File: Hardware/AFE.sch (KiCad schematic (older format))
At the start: 42 parts, among them U801 4069.HEF4069UBTT,118, U802 MCP47CXBX2

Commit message: Trying to add suppliers in Altium formats.
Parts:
- C701, C802, C804, C815, C816, C820, C822: Supplier 1 (none) -> Digi-Key; Supplier Part Number 1 (none) -> 399-6856-1-ND
- D801, D802: Supplier 1 (none) -> Mouser; Supplier Part Number 1 (none) -> 726-BB914E6327
- L801, L802: Supplier 1 (none) -> Mouser; Supplier Part Number 1 (none) -> 810-NL453232T-102JPF
- R801, R802, R803, R804, R809: Supplier 1 (none) -> Digi-Key; Supplier Part Number 1 (none) -> RHM100KDCT-ND
- U801: Supplier 1 (none) -> Digi-Key; Supplier Part Number 1 (none) -> 1727-6749-1-ND
- U801: DPN (none) -> 1727-6749-1-ND; Supplier 1 (none) -> Digi-Key; Supplier Part Number 1 (none) -> 1727-6749-1-ND
- U802: Supplier 1 (none) -> Digi-Key; Supplier Part Number 1 (none) -> MCP47CMB02-E/MF-ND
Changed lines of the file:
@@
 F 2 "OHMC2022:TSSOP14" H 3200 4550 60  0001 C CNN
 F 3 "https://assets.nexperia.com/documents/data-sheet/HEF4069UB.pdf" H 3200 4550 60  0001 C CNN
+F 4 "1727-6749-1-ND" H 3200 4550 50  0001 C CNN "DPN"
+F 5 "Digi-Key" H 3200 4550 50  0001 C CNN "Supplier 1"
+F 6 "1727-6749-1-ND" H 3200 4550 50  0001 C CNN "Supplier Part Number 1"
 	2    3200 4550
 	1    0    0    -1
@@
 F 4 "1727-6749-1-ND" H 2050 4550 50  0001 C CNN "DPN"
 F 5 "HEF4069UBTT,118" H 2050 4550 50  0001 C CNN "MPN"
+F 6 "Digi-Key" H 2050 4550 50  0001 C CNN "Supplier 1"
+F 7 "1727-6749-1-ND" H 2050 4550 50  0001 C CNN "Supplier Part Number 1"
 	3    2050 4550
 	1    0    0    -1
@@
 F 4 "NL453232T-102J-PF " H 2100 1800 50  0001 C CNN "MPN"
 F 5 "810-NL453232T-102JPF" H 2100 1800 50  0001 C CNN "MouserPN"
+F 6 "Mouser" H 2100 1800 50  0001 C CNN "Supplier 1"
+F 7 "810-NL453232T-102JPF" H 2100 1800 50  0001 C CNN "Supplier Part Number 1"
 	1    2100 1800
 	1    0    0    -1
@@
 F 4 "1727-6749-1-ND" H 3200 5250 50  0001 C CNN "DPN"
 F 5 "HEF4069UBTT,118" H 3200 5250 50  0001 C CNN "MPN"
+F 6 "Digi-Key" H 3200 5250 50  0001 C CNN "Supplier 1"
+F 7 "1727-6749-1-ND" H 3200 5250 50  0001 C CNN "Supplier Part Number 1"
 	1    3200 5250
 	1    0    0    -1
@@
 F 4 "BB 914 E6327 " H 1050 2900 50  0001 C CNN "MPN"
 F 5 "726-BB914E6327 " H 1050 2900 50  0001 C CNN "MouserPN"
+F 6 "Mouser" H 1050 2900 50  0001 C CNN "Supplier 1"
+F 7 "726-BB914E6327" H 1050 2900 50  0001 C CNN "Supplier Part Number 1"
 	1    1050 2900
 	1    0    0    -1
@@
 F 2 "OHMC2022:TSSOP14" H 3200 1100 60  0001 C CNN
 F 3 "https://assets.nexperia.com/documents/data-sheet/HEF4069UB.pdf" H 3200 1100 60  0001 C CNN
+F 4 "1727-6749-1-ND" H 3200 1100 50  0001 C CNN "DPN"
+F 5 "Digi-Key" H 3200 1100 50  0001 C CNN "Supplier 1"
+F 6 "1727-6749-1-ND" H 3200 1100 50  0001 C CNN "Supplier Part Number 1"
 	5    3200 1100
 	1    0    0    -1
@@
 F 2 "OHMC2022:TSSOP14" H 3200 1800 60  0001 C CNN
 F 3 "https://assets.nexperia.com/documents/data-sheet/HEF4069UB.pdf" H 3200 1800 60  0001 C CNN
+F 4 "1727-6749-1-ND" H 3200 1800 50  0001 C CNN "DPN"
+F 5 "Digi-Key" H 3200 1800 50  0001 C CNN "Supplier 1"
+F 6 "1727-6749-1-ND" H 3200 1800 50  0001 C CNN "Supplier Part Number 1"
 	6    3200 1800
 	1    0    0    -1
@@
 F 2 "OHMC2022:TSSOP14" H 2050 1100 60  0001 C CNN
 F 3 "https://assets.nexperia.com/documents/data-sheet/HEF4069UB.pdf" H 2050 1100 60  0001 C CNN
+F 4 "1727-6749-1-ND" H 2050 1100 50  0001 C CNN "DPN"
+F 5 "Digi-Key" H 2050 1100 50  0001 C CNN "Supplier 1"
+F 6 "1727-6749-1-ND" H 2050 1100 50  0001 C CNN "Supplier Part Number 1"
 	4    2050 1100
 	1    0    0    -1
@@
 F 4 "MCP47CMB02-E/MF-ND" H 7900 5000 50  0001 C CNN "DPN"
 F 5 "MCP47CMB02-E/MF" H 7850 4850 50  0001 C CNN "MPN"
+F 6 "Digi-Key" H 7450 4400 50  0001 C CNN "Supplier 1"
+F 7 "MCP47CMB02-E/MF-ND" H 7450 4400 50  0001 C CNN "Supplier Part Number 1"
 	1    7450 4400
 	1    0    0    -1
@@
 F 4 "BB 914 E6327 " H 1050 6350 50  0001 C CNN "MPN"
 F 5 "726-BB914E6327 " H 1050 6350 50  0001 C CNN "MouserPN"
+F 6 "Mouser" H 1050 6350 50  0001 C CNN "Supplier 1"
+F 7 "726-BB914E6327" H 1050 6350 50  0001 C CNN "Supplier Part Number 1"
 	1    1050 6350
 	1    0    0    -1
@@
 F 4 "NL453232T-102J-PF " H 2100 5250 50  0001 C CNN "MPN"
 F 5 "810-NL453232T-102JPF" H 2100 5250 50  0001 C CNN "MouserPN"
+F 6 "Mouser" H 2100 5250 50  0001 C CNN "Supplier 1"
+F 7 "810-NL453232T-102JPF" H 2100 5250 50  0001 C CNN "Supplier Part Number 1"
 	1    2100 5250
 	1    0    0    -1
@@
 F 4 "HEF4069UBTT,118" H 9000 1350 50  0001 C CNN "MPN"
 F 5 "1727-6749-1-ND" H 9000 1350 50  0001 C CNN "DPN"
+F 6 "Digi-Key" H 9000 1350 50  0001 C CNN "Supplier 1"
+F 7 "1727-6749-1-ND" H 9000 1350 50  0001 C CNN "Supplier Part Number 1"
 	7    9000 1350
 	1    0    0    -1
@@
 F 5 "ESR03EZPJ104" H 1450 3550 50  0001 C CNN "MPN"
 F 6 "RHM100KDCT-ND" H 1450 3550 50  0001 C CNN "DPN"
+F 7 "Digi-Key" H 1450 3550 50  0001 C CNN "Supplier 1"
+F 8 "RHM100KDCT-ND" H 1450 3550 50  0001 C CNN "Supplier Part Number 1"
 	1    1450 3550
 	0    -1   -1   0
@@
 F 5 "ESR03EZPJ104" H 1050 3300 50  0001 C CNN "MPN"
 F 6 "RHM100KDCT-ND" H 1050 3300 50  0001 C CNN "DPN"
+F 7 "Digi-Key" H 1050 3300 50  0001 C CNN "Supplier 1"
+F 8 "RHM100KDCT-ND" H 1050 3300 50  0001 C CNN "Supplier Part Number 1"
 	1    1050 3300
 	1    0    0    -1
@@
 F 5 "ESR03EZPJ104" H 6250 1200 50  0001 C CNN "MPN"
 F 6 "RHM100KDCT-ND" H 6250 1200 50  0001 C CNN "DPN"
+F 7 "Digi-Key" H 6250 1200 50  0001 C CNN "Supplier 1"
+F 8 "RHM100KDCT-ND" H 6250 1200 50  0001 C CNN "Supplier Part Number 1"
 	1    6250 1200
 	0    -1   -1   0
@@
 F 5 "ESR03EZPJ104" H 1550 7000 50  0001 C CNN "MPN"
 F 6 "RHM100KDCT-ND" H 1550 7000 50  0001 C CNN "DPN"
+F 7 "Digi-Key" H 1550 7000 50  0001 C CNN "Supplier 1"
+F 8 "RHM100KDCT-ND" H 1550 7000 50  0001 C CNN "Supplier Part Number 1"
 	1    1550 7000
 	0    -1   -1   0
@@
 F 5 "ESR03EZPJ104" H 1050 6750 50  0001 C CNN "MPN"
 F 6 "RHM100KDCT-ND" H 1050 6750 50  0001 C CNN "DPN"
+F 7 "Digi-Key" H 1050 6750 50  0001 C CNN "Supplier 1"
+F 8 "RHM100KDCT-ND" H 1050 6750 50  0001 C CNN "Supplier Part Number 1"
 	1    1050 6750
 	1    0    0    -1
@@
 F 7 "0603" H 6365 5709 50  0000 L CNN "Pkg"
 F 8 "X7R" H 6365 5618 50  0000 L CNN "TCoff"
+F 9 "Digi-Key" H 6250 5800 50  0001 C CNN "Supplier 1"
+F 10 "399-6856-1-ND" H 6250 5800 50  0001 C CNN "Supplier Part Number 1"
 	1    6250 5800
 	1    0    0    -1
@@
 F 7 "0603" H 6765 5709 50  0000 L CNN "Pkg"
 F 8 "X7R" H 6765 5618 50  0000 L CNN "TCoff"
+F 9 "Digi-Key" H 6650 5800 50  0001 C CNN "Supplier 1"
+F 10 "399-6856-1-ND" H 6650 5800 50  0001 C CNN "Supplier Part Number 1"
 	1    6650 5800
 	1    0    0    -1
@@
 F 7 "0603" H 7015 1259 50  0000 L CNN "Pkg"
 F 8 "X7R" H 7015 1168 50  0000 L CNN "TCoff"
+F 9 "Digi-Key" H 6900 1350 50  0001 C CNN "Supplier 1"
+F 10 "399-6856-1-ND" H 6900 1350 50  0001 C CNN "Supplier Part Number 1"
 	1    6900 1350
 	1    0    0    -1
@@
 F 7 "0603" H 7615 1259 50  0000 L CNN "Pkg"
 F 8 "X7R" H 7615 1168 50  0000 L CNN "TCoff"
+F 9 "Digi-Key" H 7500 1350 50  0001 C CNN "Supplier 1"
+F 10 "399-6856-1-ND" H 7500 1350 50  0001 C CNN "Supplier Part Number 1"
 	1    7500 1350
 	1    0    0    -1
@@
 F 7 "0603" H 6065 1309 50  0000 L CNN "Pkg"
 F 8 "X7R" H 6065 1218 50  0000 L CNN "TCoff"
+F 9 "Digi-Key" H 5950 1400 50  0001 C CNN "Supplier 1"
+F 10 "399-6856-1-ND" H 5950 1400 50  0001 C CNN "Supplier Part Number 1"
 	1    5950 1400
 	-1   0    0    -1
@@
 F 7 "0603" H 1165 7109 50  0000 L CNN "Pkg"
 F 8 "X7R" H 1165 7018 50  0000 L CNN "TCoff"
+F 9 "Digi-Key" H 1050 7200 50  0001 C CNN "Supplier 1"
+F 10 "399-6856-1-ND" H 1050 7200 50  0001 C CNN "Supplier Part Number 1"
 	1    1050 7200
 	-1   0    0    -1
@@
 F 7 "0603" H 1165 3659 50  0000 L CNN "Pkg"
 F 8 "X7R" H 1165 3568 50  0000 L CNN "TCoff"
+F 9 "Digi-Key" H 1050 3750 50  0001 C CNN "Supplier 1"
+F 10 "399-6856-1-ND" H 1050 3750 50  0001 C CNN "Supplier Part Number 1"
 	1    1050 3750
 	-1   0    0    -1

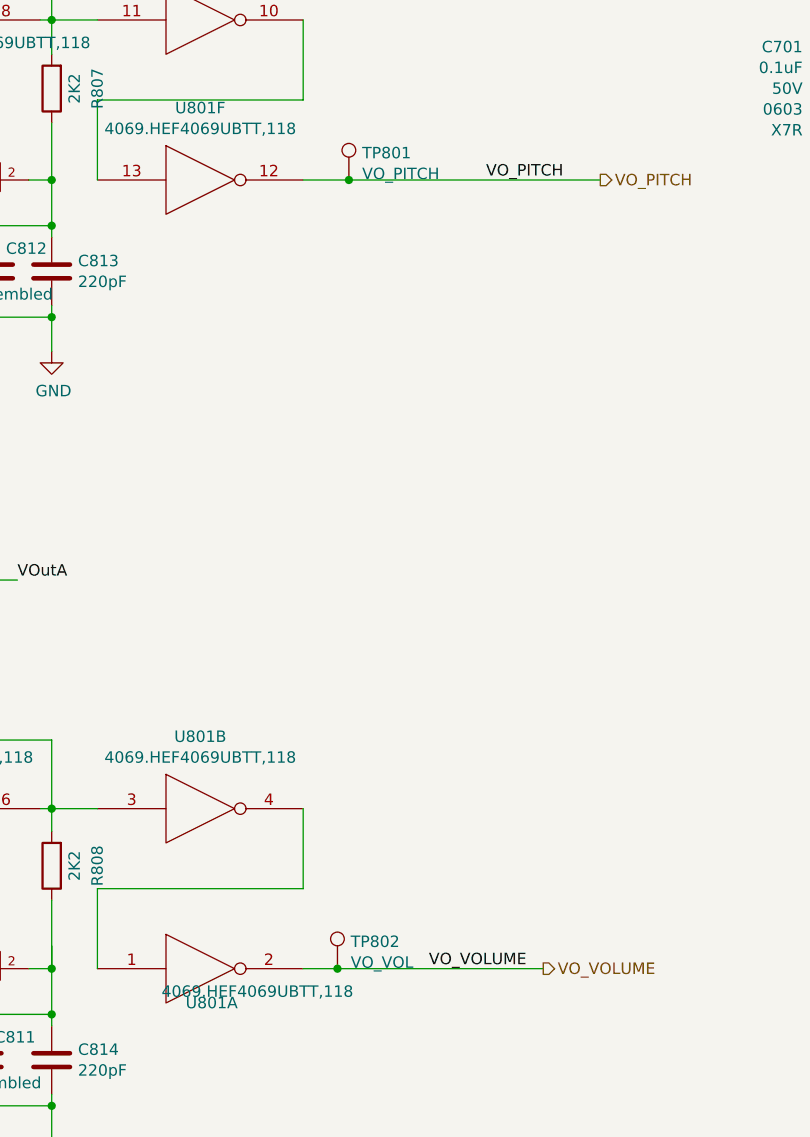
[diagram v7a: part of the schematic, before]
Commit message: Routing going in now.
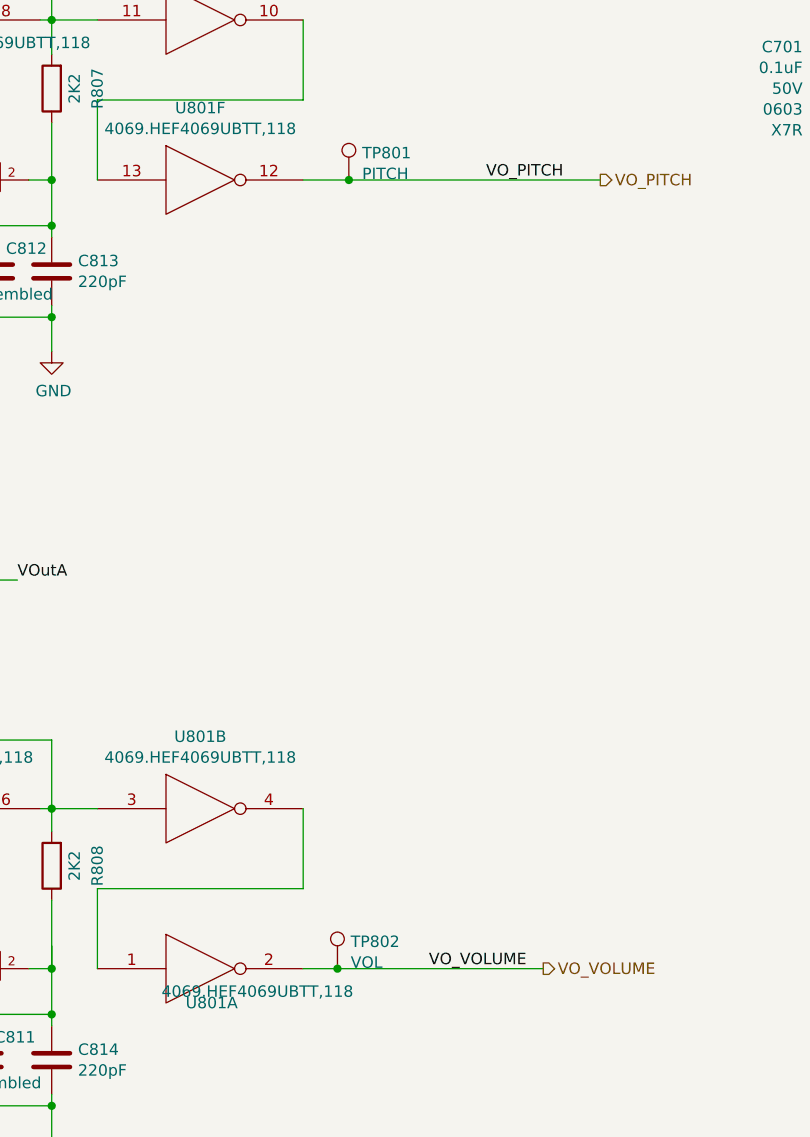
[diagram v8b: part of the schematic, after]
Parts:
- TP801: value VO_PITCH -> PITCH; footprint TestPoint:TestPoint_THTPad_D1.5mm_Drill0.7mm -> OHMC2022:TestPoint_THTPad_D1.5mm_Drill0.7mm
- TP802: value VO_VOL -> VOL; footprint TestPoint:TestPoint_THTPad_D1.5mm_Drill0.7mm -> OHMC2022:TestPoint_THTPad_D1.5mm_Drill0.7mm
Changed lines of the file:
@@
 P 3850 1800
 F 0 "TP801" H 3908 1918 50  0000 L CNN
-F 1 "VO_PITCH" H 3908 1827 50  0000 L CNN
-F 2 "TestPoint:TestPoint_THTPad_D1.5mm_Drill0.7mm" H 4050 1800 50  0001 C CNN
+F 1 "PITCH" H 3908 1827 50  0000 L CNN
+F 2 "OHMC2022:TestPoint_THTPad_D1.5mm_Drill0.7mm" H 4050 1800 50  0001 C CNN
 F 3 "~" H 4050 1800 50  0001 C CNN
 	1    3850 1800
@@
 P 3800 5250
 F 0 "TP802" H 3858 5368 50  0000 L CNN
-F 1 "VO_VOL" H 3858 5277 50  0000 L CNN
-F 2 "TestPoint:TestPoint_THTPad_D1.5mm_Drill0.7mm" H 4000 5250 50  0001 C CNN
+F 1 "VOL" H 3858 5277 50  0000 L CNN
+F 2 "OHMC2022:TestPoint_THTPad_D1.5mm_Drill0.7mm" H 4000 5250 50  0001 C CNN
 F 3 "~" H 4000 5250 50  0001 C CNN
 	1    3800 5250
